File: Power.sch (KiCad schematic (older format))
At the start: 40 parts, among them U1 LP2985-3.3, U3 LP2985-3.3, U4 MP4560_QFN10, U5 MP4560_QFN10

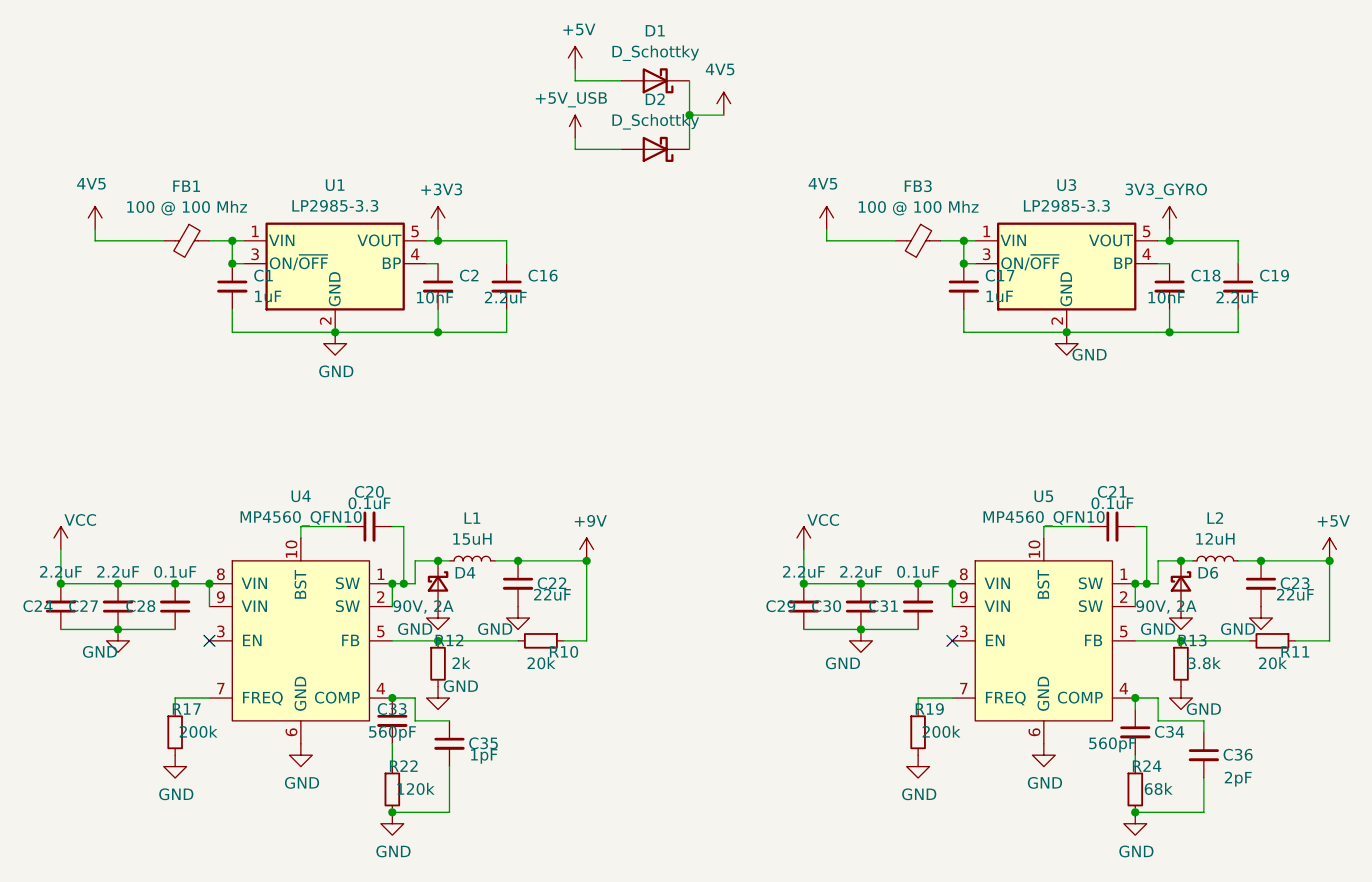
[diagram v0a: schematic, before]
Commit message: Changed to 20x20 form factor
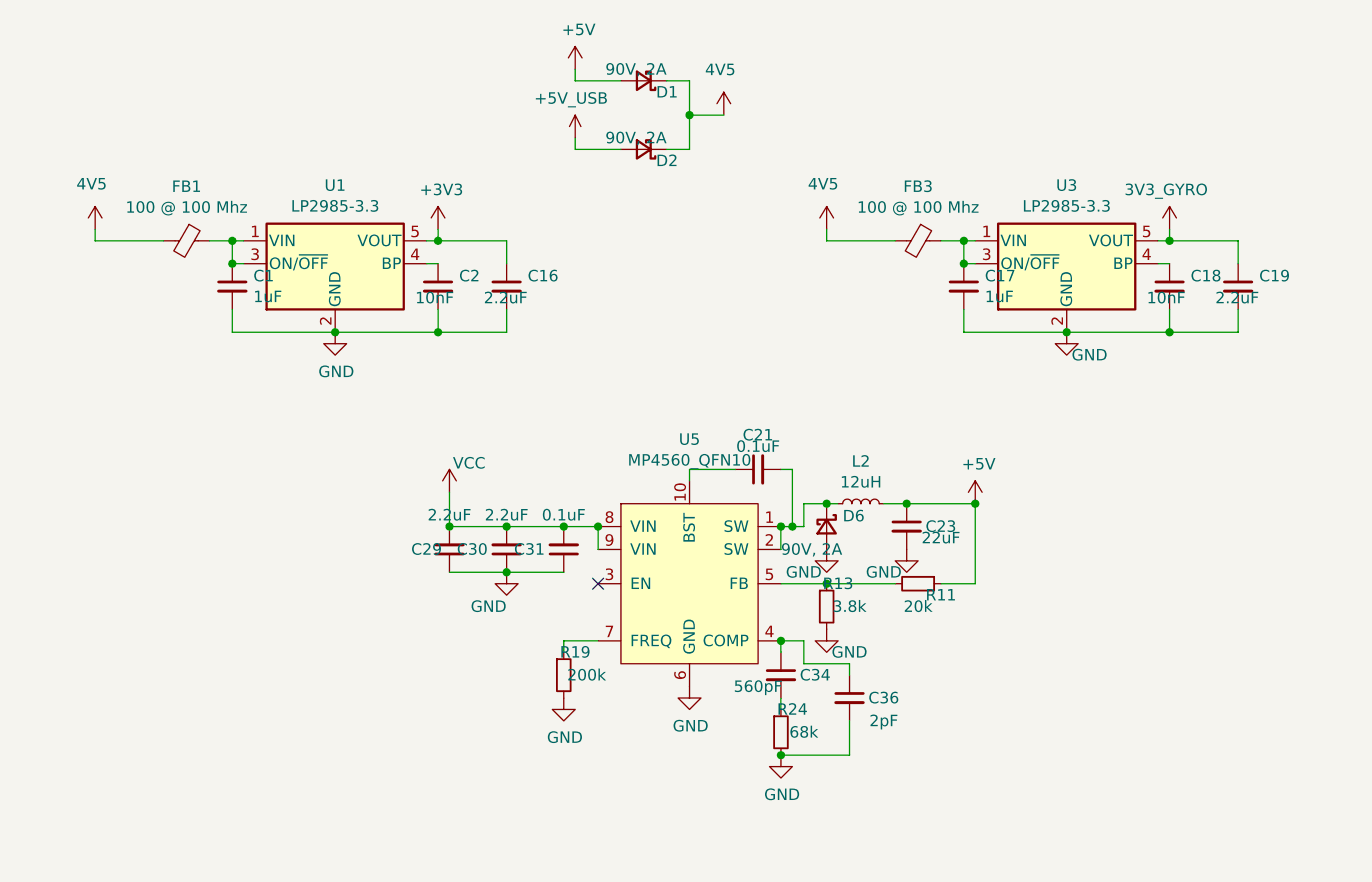
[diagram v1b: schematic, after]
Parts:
- removed C20, C28: 0.1uF, Capacitor_SMD:C_0402_1005Metric, symbol Device:C_Small
- removed C22: 22uF, Capacitor_SMD:C_0603_1608Metric, symbol Device:C_Small
- removed C24, C27: 2.2uF, Capacitor_SMD:C_0603_1608Metric, symbol Device:C_Small
- removed C33: 560pF, Capacitor_SMD:C_0402_1005Metric, symbol Device:C_Small
- removed C35: 1pF, Capacitor_SMD:C_0402_1005Metric, symbol Device:C_Small
- removed D1, D2: D_Schottky, Footprints:SBR3U30P1-7, symbol Device:D_Schottky
- removed D4: 90V, 2A, Diode_SMD:D_SOD-123F, symbol Device:D_Schottky_Small
- removed L1: 15uH, Inductor_SMD:L_XGL4030, symbol Device:L_Small
- removed R10: 20k, Resistor_SMD:R_0402_1005Metric, symbol Device:R_Small
- removed R12: 2k, Resistor_SMD:R_0402_1005Metric, symbol Device:R_Small
- removed R17: 200k, Resistor_SMD:R_0402_1005Metric, symbol Device:R_Small
- removed R22: 120k, Resistor_SMD:R_0402_1005Metric, symbol Device:R_Small
- removed U4: MP4560_QFN10, Package_DFN_QFN:DFN-10-1EP_3x3mm_P0.5mm_EP1.7x2.5mm, symbol Regulator_Switching:MP4560_QFN10
- added D1, D2: 90V, 2A, Diode_SMD:D_SOD-123F, symbol Device:D_Schottky_Small
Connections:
- net +5V: now also D1.2 (A)
- net +5V_USB: now also D2.2 (A)
- net 4V5: now also D1.1 (K), D2.1 (K)
- no-connect marks 2 -> 1
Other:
- moved on the sheet: C21, C23, C29, C30, C31, C34, C36, D6, L2, R11, R13, R19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

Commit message: Changes made
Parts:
- removed C29: 2.2uF, Capacitor_SMD:C_0603_1608Metric, symbol Device:C_Small
- removed U5: MP4560_QFN10, Package_DFN_QFN:DFN-10-1EP_3x3mm_P0.5mm_EP1.7x2.5mm, symbol Regulator_Switching:MP4560_QFN10
- added C12: 0.1uF, Capacitor_SMD:C_0402_1005Metric, symbol Device:C_Small
- added U5: MP4561_QFN10, Package_DFN_QFN:DFN-10-1EP_3x3mm_P0.5mm_EP1.7x2.5mm, symbol Regulator_Switching:MP4561_QFN10
- C30: value 2.2uF -> 4.7uF
- C36: value 2pF -> 1pF
- L2: value 12uH -> 15uH
- R19: value 200k -> 195k
- R24: value 68k -> 88.7k
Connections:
- net GND: now also C12.1, U5.6 (GND)
- net VCC: now also U5.9 (VIN)
- net at C34.1, C36.1: now also U5.4 (COMP)
- net at R11.2, R13.1: now also U5.5 (FB)
- net at C21.2, D6.1 (K), L2.1: now also U5.1 (SW), U5.2 (SW)
- net at R19.1: now also U5.7 (FREQ)
- net at C21.1: now also U5.10 (BST)
- new net: C12.2, U5.8 (SS)
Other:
- moved on the sheet: C30, C31
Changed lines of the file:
@@
 	6000 5100 6000 5150
 Wire Wire Line
-	4800 4350 5050 4350
-Connection ~ 4800 4350
-Wire Wire Line
-	4550 4350 4800 4350
-Connection ~ 4550 4350
-Wire Wire Line
-	4800 4550 5050 4550
-Connection ~ 4800 4550
-Wire Wire Line
-	4550 4550 4800 4550
-Wire Wire Line
-	4550 4350 4550 4200
+	4550 4450 4800 4450
+Connection ~ 4550 4450
+Wire Wire Line
+	4550 4650 4800 4650
+Connection ~ 4550 4650
 $Comp
 L Device:C_Small C?
 U 1 1 60967A9B
-P 5050 4450
+P 4800 4550
 AR Path="/60967A9B" Ref="C?"  Part="1"
 AR Path="/6094AC2B/60967A9B" Ref="C31"  Part="1"
-F 0 "C31" H 5200 4450 50  0000 C CNN
-F 1 "0.1uF" H 5050 4300 50  0000 C CNN
-F 2 "Capacitor_SMD:C_0402_1005Metric" H 5050 4450 50  0001 C CNN
-F 3 "~" H 5050 4450 50  0001 C CNN
-	1    5050 4450
+F 0 "C31" H 4900 4600 50  0000 C CNN
+F 1 "0.1uF" H 4900 4500 50  0000 C CNN
+F 2 "Capacitor_SMD:C_0402_1005Metric" H 4800 4550 50  0001 C CNN
+F 3 "~" H 4800 4550 50  0001 C CNN
+	1    4800 4550
 	-1   0    0    1
 $EndComp
@@
 L Device:C_Small C?
 U 1 1 60967AA1
-P 4800 4450
+P 4550 4550
 AR Path="/60967AA1" Ref="C?"  Part="1"
 AR Path="/6094AC2B/60967AA1" Ref="C30"  Part="1"
-F 0 "C30" H 4950 4450 50  0000 C CNN
-F 1 "2.2uF" H 4800 4300 50  0000 C CNN
-F 2 "Capacitor_SMD:C_0603_1608Metric" H 4800 4450 50  0001 C CNN
-F 3 "~" H 4800 4450 50  0001 C CNN
-	1    4800 4450
+F 0 "C30" H 4650 4600 50  0000 C CNN
+F 1 "4.7uF" H 4650 4500 50  0000 C CNN
+F 2 "Capacitor_SMD:C_0603_1608Metric" H 4550 4550 50  0001 C CNN
+F 3 "~" H 4550 4550 50  0001 C CNN
+	1    4550 4550
 	-1   0    0    1
 $EndComp
@@
 AR Path="/6094AC2B/60967AAE" Ref="C36"  Part="1"
 F 0 "C36" H 6450 5100 50  0000 C CNN
-F 1 "2pF" H 6450 5000 50  0000 C CNN
+F 1 "1pF" H 6450 5000 50  0000 C CNN
 F 2 "Capacitor_SMD:C_0402_1005Metric" H 6300 5100 50  0001 C CNN
 F 3 "~" H 6300 5100 50  0001 C CNN
@@
 AR Path="/6094AC2B/60967ACC" Ref="R24"  Part="1"
 F 0 "R24" H 6050 5350 50  0000 C CNN
-F 1 "68k" H 6100 5250 50  0000 C CNN
+F 1 "88.7k" H 6100 5250 50  0000 C CNN
 F 2 "Resistor_SMD:R_0402_1005Metric" H 6000 5250 50  0001 C CNN
 F 3 "~" H 6000 5250 50  0001 C CNN
@@
 AR Path="/6094AC2B/60967B08" Ref="L2"  Part="1"
 F 0 "L2" V 6535 4250 50  0000 C CNN
-F 1 "12uH" V 6444 4250 50  0000 C CNN
+F 1 "15uH" V 6444 4250 50  0000 C CNN
 F 2 "Inductor_SMD:L_XGL4030" H 6350 4250 50  0001 C CNN
 F 3 "~" H 6350 4250 50  0001 C CNN
@@
 AR Path="/6094AC2B/60967B1F" Ref="R19"  Part="1"
 F 0 "R19" H 5100 5100 50  0000 C CNN
-F 1 "200k" H 5150 5000 50  0000 C CNN
+F 1 "195k" H 5150 5000 50  0000 C CNN
 F 2 "Resistor_SMD:R_0402_1005Metric" H 5050 5000 50  0001 C CNN
 F 3 "~" H 5050 5000 50  0001 C CNN
@@
 L power:GND #PWR?
 U 1 1 60967B25
-P 4800 4550
+P 4550 4650
 AR Path="/60967B25" Ref="#PWR?"  Part="1"
 AR Path="/6094AC2B/60967B25" Ref="#PWR0119"  Part="1"
-F 0 "#PWR0119" H 4800 4300 50  0001 C CNN
-F 1 "GND" H 4800 4400 50  0000 R CNN
-F 2 "" H 4800 4550 50  0001 C CNN
-F 3 "" H 4800 4550 50  0001 C CNN
-	1    4800 4550
+F 0 "#PWR0119" H 4550 4400 50  0001 C CNN
+F 1 "GND" H 4550 4500 50  0000 R CNN
+F 2 "" H 4550 4650 50  0001 C CNN
+F 3 "" H 4550 4650 50  0001 C CNN
+	1    4550 4650
 	1    0    0    -1
 $EndComp
@@
 $EndComp
 $Comp
-L Device:C_Small C?
-U 1 1 60967B31
-P 4550 4450
-AR Path="/60967B31" Ref="C?"  Part="1"
-AR Path="/6094AC2B/60967B31" Ref="C29"  Part="1"
-F 0 "C29" H 4650 4450 50  0000 C CNN
-F 1 "2.2uF" H 4550 4300 50  0000 C CNN
-F 2 "Capacitor_SMD:C_0603_1608Metric" H 4550 4450 50  0001 C CNN
-F 3 "~" H 4550 4450 50  0001 C CNN
-	1    4550 4450
-	-1   0    0    1
-$EndComp
-$Comp
 L power:VCC #PWR?
 U 1 1 60967B37
-P 4550 4200
+P 4550 4450
 AR Path="/60967B37" Ref="#PWR?"  Part="1"
 AR Path="/6094AC2B/60967B37" Ref="#PWR0120"  Part="1"
-F 0 "#PWR0120" H 4550 4050 50  0001 C CNN
-F 1 "VCC" H 4565 4327 50  0000 L CNN
-F 2 "" H 4550 4200 50  0001 C CNN
-F 3 "" H 4550 4200 50  0001 C CNN
-	1    4550 4200
+F 0 "#PWR0120" H 4550 4300 50  0001 C CNN
+F 1 "VCC" H 4565 4577 50  0000 L CNN
+F 2 "" H 4550 4450 50  0001 C CNN
+F 3 "" H 4550 4450 50  0001 C CNN
+	1    4550 4450
 	1    0    0    -1
 $EndComp
@@
 	3000 3100 3300 3100
 $Comp
-L power:+5V_USB #PWR?
-U 1 1 6097D22F
-P 5100 2650
-AR Path="/6097D22F" Ref="#PWR?"  Part="1"
-AR Path="/6094AC2B/6097D22F" Ref="#PWR0124"  Part="1"
-F 0 "#PWR0124" H 5100 2550 50  0001 C CNN
-F 1 "+5V_USB" H 5082 2823 50  0000 C CNN
-F 2 "" H 5100 2650 50  0001 C CNN
-F 3 "" H 5100 2650 50  0001 C CNN
-	1    5100 2650
-	1    0    0    -1
-$EndComp
-Wire Wire Line
-	5100 2350 5100 2400
-Wire Wire Line
-	5100 2400 5300 2400
-$Comp
-L power:4V5 #PWR?
-U 1 1 6097D237
-P 5750 2600
-AR Path="/6097D237" Ref="#PWR?"  Part="1"
-AR Path="/6094AC2B/6097D237" Ref="#PWR0125"  Part="1"
-F 0 "#PWR0125" H 5925 2675 50  0001 C CNN
-F 1 "4V5" H 5735 2848 50  0000 C CNN
-F 2 "" H 5750 2600 50  0001 C CNN
-F 3 "" H 5750 2600 50  0001 C CNN
-	1    5750 2600
-	1    0    0    -1
-$EndComp
-Wire Wire Line
-	5100 2650 5100 2700
-Wire Wire Line
-	5100 2700 5300 2700
-Wire Wire Line
-	5600 2400 5600 2550
-Wire Wire Line
-	5600 2550 5750 2550
-Wire Wire Line
-	5600 2700 5600 2550
-Connection ~ 5600 2550
-$Comp
-L power:+5V #PWR?
-U 1 1 6097D249
-P 5100 2350
-AR Path="/6097D249" Ref="#PWR?"  Part="1"
-AR Path="/6094AC2B/6097D249" Ref="#PWR0126"  Part="1"
-F 0 "#PWR0126" H 5100 2200 50  0001 C CNN
-F 1 "+5V" H 5115 2523 50  0000 C CNN
-F 2 "" H 5100 2350 50  0001 C CNN
-F 3 "" H 5100 2350 50  0001 C CNN
-	1    5100 2350
-	1    0    0    -1
-$EndComp
-$Comp
 L power:4V5 #PWR?
 U 1 1 6097D24F
@@
 	1    0    0    -1
 $EndComp
-Wire Wire Line
-	5050 4350 5200 4350
-Connection ~ 5050 4350
 NoConn ~ 5200 4600
-$Comp
-L Regulator_Switching:MP4560_QFN10 U5
-U 1 1 60C27B5F
-P 5600 4600
-F 0 "U5" H 5600 5231 50  0000 C CNN
-F 1 "MP4560_QFN10" H 5600 5140 50  0000 C CNN
-F 2 "Package_DFN_QFN:DFN-10-1EP_3x3mm_P0.5mm_EP1.7x2.5mm" H 5600 4900 50  0001 C CNN
-F 3 "" H 5600 4900 50  0001 C CNN
-	1    5600 4600
-	1    0    0    -1
-$EndComp
-Connection ~ 6000 4850
-Wire Wire Line
-	5200 4450 5200 4350
-Connection ~ 5200 4350
 Wire Wire Line
 	6000 4450 6000 4350
-Connection ~ 6000 4350
+Wire Wire Line
+	5500 2700 5600 2700
+Wire Wire Line
+	5500 2400 5600 2400
+$Comp
+L Device:D_Schottky_Small D?
+U 1 1 60B52C20
+P 5400 2700
+AR Path="/60B52C20" Ref="D?"  Part="1"
+AR Path="/6094AC2B/60B52C20" Ref="D2"  Part="1"
+F 0 "D2" H 5250 2750 50  0000 L CNN
+F 1 "90V, 2A" H 5300 2650 50  0000 L CNN
+F 2 "Diode_SMD:D_SOD-123F" V 5400 2700 50  0001 C CNN
+F 3 "~" V 5400 2700 50  0001 C CNN
+	1    5400 2700
+	-1   0    0    1
+$EndComp
 $Comp
 L Device:D_Schottky_Small D?
@@
 $EndComp
 $Comp
-L Device:D_Schottky_Small D?
-U 1 1 60B52C20
-P 5400 2700
-AR Path="/60B52C20" Ref="D?"  Part="1"
-AR Path="/6094AC2B/60B52C20" Ref="D2"  Part="1"
-F 0 "D2" H 5250 2750 50  0000 L CNN
-F 1 "90V, 2A" H 5300 2650 50  0000 L CNN
-F 2 "Diode_SMD:D_SOD-123F" V 5400 2700 50  0001 C CNN
-F 3 "~" V 5400 2700 50  0001 C CNN
-	1    5400 2700
+L power:+5V #PWR?
+U 1 1 6097D249
+P 5100 2350
+AR Path="/6097D249" Ref="#PWR?"  Part="1"
+AR Path="/6094AC2B/6097D249" Ref="#PWR0126"  Part="1"
+F 0 "#PWR0126" H 5100 2200 50  0001 C CNN
+F 1 "+5V" H 5115 2523 50  0000 C CNN
+F 2 "" H 5100 2350 50  0001 C CNN
+F 3 "" H 5100 2350 50  0001 C CNN
+	1    5100 2350
+	1    0    0    -1
+$EndComp
+Wire Wire Line
+	5600 2700 5600 2550
+Wire Wire Line
+	5600 2550 5750 2550
+Connection ~ 5600 2550
+Wire Wire Line
+	5600 2400 5600 2550
+Wire Wire Line
+	5100 2700 5300 2700
+Wire Wire Line
+	5100 2650 5100 2700
+$Comp
+L power:4V5 #PWR?
+U 1 1 6097D237
+P 5750 2600
+AR Path="/6097D237" Ref="#PWR?"  Part="1"
+AR Path="/6094AC2B/6097D237" Ref="#PWR0125"  Part="1"
+F 0 "#PWR0125" H 5925 2675 50  0001 C CNN
+F 1 "4V5" H 5735 2848 50  0000 C CNN
+F 2 "" H 5750 2600 50  0001 C CNN
+F 3 "" H 5750 2600 50  0001 C CNN
+	1    5750 2600
+	1    0    0    -1
+$EndComp
+Wire Wire Line
+	5100 2400 5300 2400
+Wire Wire Line
+	5100 2350 5100 2400
+$Comp
+L power:+5V_USB #PWR?
+U 1 1 6097D22F
+P 5100 2650
+AR Path="/6097D22F" Ref="#PWR?"  Part="1"
+AR Path="/6094AC2B/6097D22F" Ref="#PWR0124"  Part="1"
+F 0 "#PWR0124" H 5100 2550 50  0001 C CNN
+F 1 "+5V_USB" H 5082 2823 50  0000 C CNN
+F 2 "" H 5100 2650 50  0001 C CNN
+F 3 "" H 5100 2650 50  0001 C CNN
+	1    5100 2650
+	1    0    0    -1
+$EndComp
+Wire Wire Line
+	4800 4450 5200 4450
+Connection ~ 4800 4450
+$Comp
+L Device:C_Small C?
+U 1 1 60D96081
+P 4800 5000
+AR Path="/60D96081" Ref="C?"  Part="1"
+AR Path="/6094AC2B/60D96081" Ref="C12"  Part="1"
+F 0 "C12" H 4900 5050 50  0000 C CNN
+F 1 "0.1uF" H 4900 4950 50  0000 C CNN
+F 2 "Capacitor_SMD:C_0402_1005Metric" H 4800 5000 50  0001 C CNN
+F 3 "~" H 4800 5000 50  0001 C CNN
+	1    4800 5000
 	-1   0    0    1
 $EndComp
 Wire Wire Line
-	5500 2400 5600 2400
-Wire Wire Line
-	5500 2700 5600 2700
+	5050 4350 5200 4350
+$Comp
+L power:GND #PWR?
+U 1 1 60D991B3
+P 4800 5100
+AR Path="/60D991B3" Ref="#PWR?"  Part="1"
+AR Path="/6094AC2B/60D991B3" Ref="#PWR0105"  Part="1"
+F 0 "#PWR0105" H 4800 4850 50  0001 C CNN
+F 1 "GND" H 4805 4927 50  0000 C CNN
+F 2 "" H 4800 5100 50  0001 C CNN
+F 3 "" H 4800 5100 50  0001 C CNN
+	1    4800 5100
+	1    0    0    -1
+$EndComp
+Wire Wire Line
+	5050 4750 4800 4750
+Wire Wire Line
+	4800 4750 4800 4900
+Wire Wire Line
+	5050 4350 5050 4750
+$Comp
+L Regulator_Switching:MP4561_QFN10 U5
+U 1 1 60DB77BA
+P 5600 4600
+F 0 "U5" H 5600 5231 50  0000 C CNN
+F 1 "MP4561_QFN10" H 5600 5140 50  0000 C CNN
+F 2 "Package_DFN_QFN:DFN-10-1EP_3x3mm_P0.5mm_EP1.7x2.5mm" H 5600 4600 50  0001 C CNN
+F 3 "" H 5600 4600 50  0001 C CNN
+	1    5600 4600
+	1    0    0    -1
+$EndComp
+Connection ~ 6000 4350
+Connection ~ 6000 4850
 $EndSCHEMATC
